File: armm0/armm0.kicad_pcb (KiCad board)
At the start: 2 copper layers, 25.4 x 52.1 mm, 20 parts, among them J1 Conn_02x10_Odd_Even, J4 Conn_02x08_Odd_Even, J5 Conn_02x08_Odd_Even, J6 Conn_01x05_Male, J7 Conn_01x05_Male, J8 Conn_01x03_Male, U1 STM32F070F6Px, U2 LD1117S33TR_SOT223

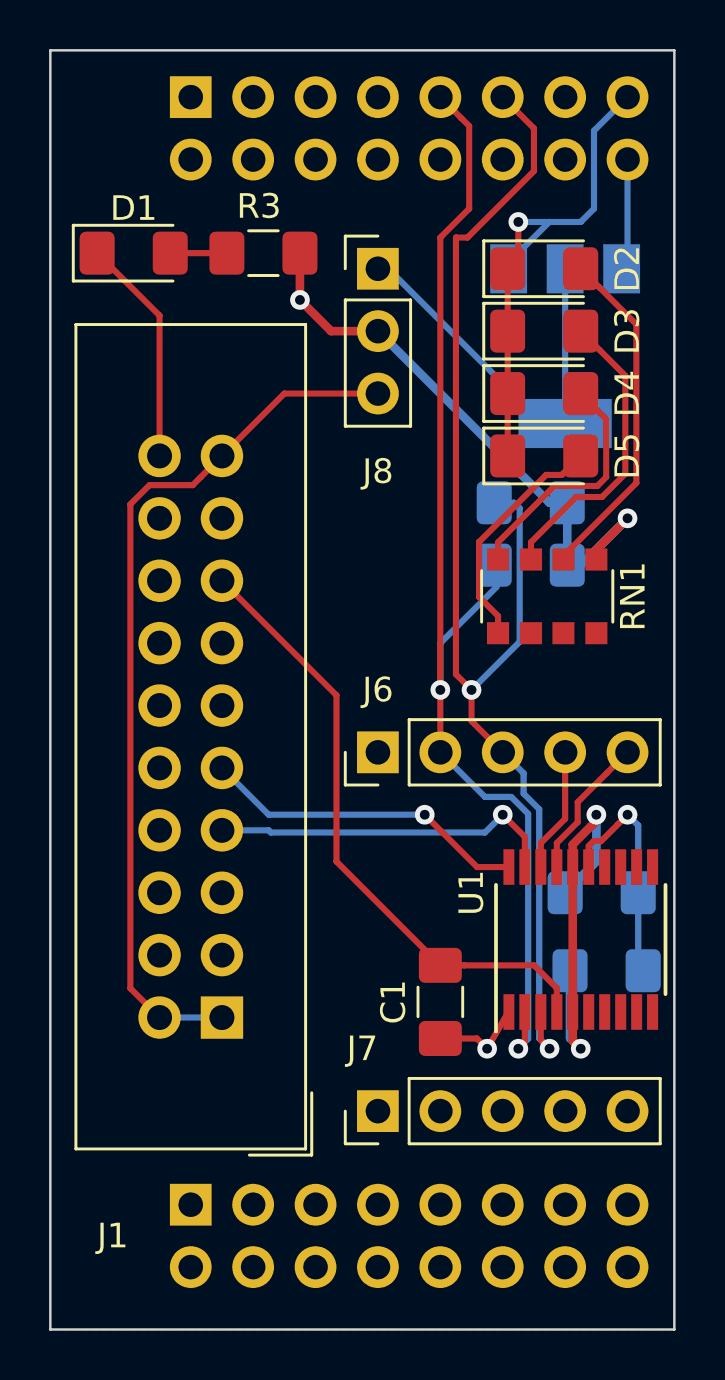
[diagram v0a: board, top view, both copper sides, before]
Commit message: pcb: Fixed header distance
Signed-off-by: Ben Lancaster <bdl@live.co.uk>
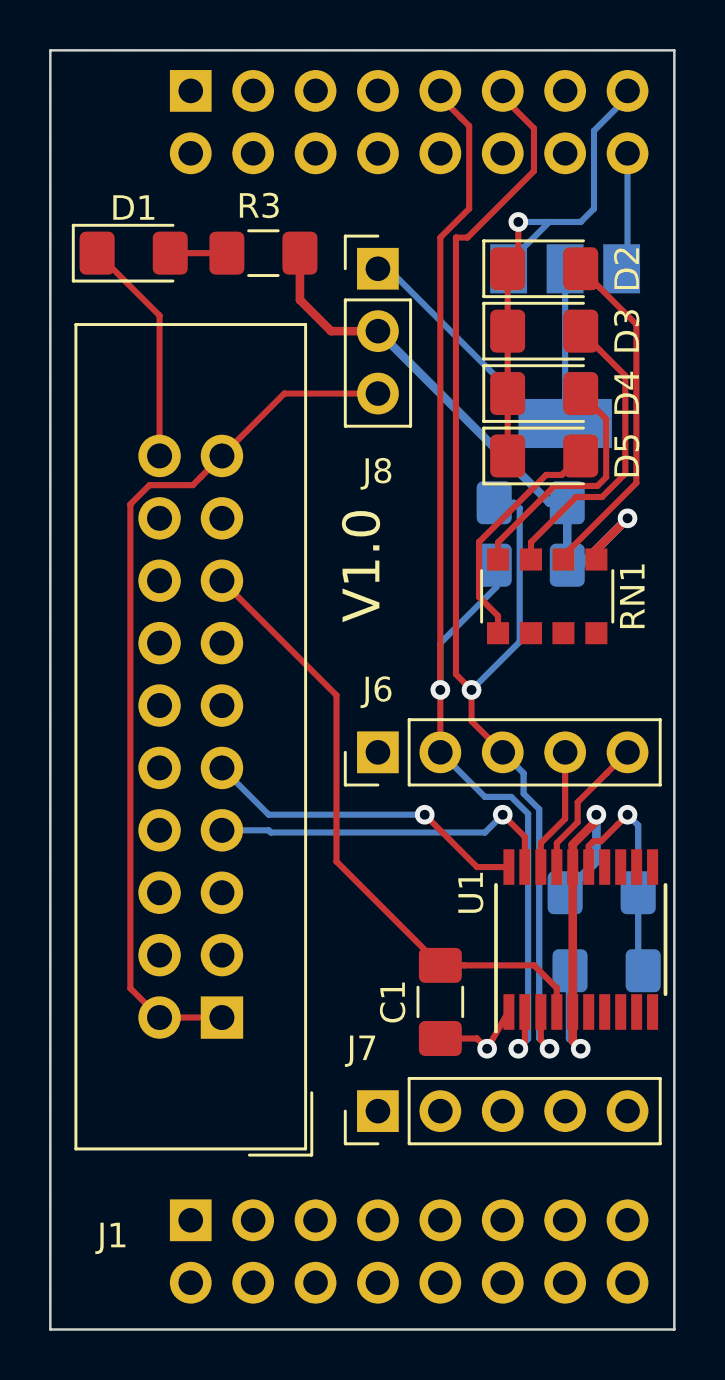
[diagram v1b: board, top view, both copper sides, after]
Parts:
- moved J4 0.63 mm to (80.6, 78.7)
- moved J5 0.25 mm to (80.6, 32.8)
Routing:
- net +3V3: vias 4 -> 3
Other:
- board text added: "BDL"
- board text added: "V1.0"
- board text removed: "+3v3"
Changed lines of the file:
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@@
   (general
     (thickness 1.6)
-    (drawings 12)
-    (tracks 170)
+    (drawings 14)
+    (tracks 169)
     (zones 0)
     (modules 20)
@@
     (34 B.Paste user)
     (35 F.Paste user)
-    (36 B.SilkS user hide)
+    (36 B.SilkS user)
     (37 F.SilkS user)
     (38 B.Mask user)
     (39 F.Mask user)
-    (40 Dwgs.User user)
+    (40 Dwgs.User user hide)
     (41 Cmts.User user)
     (42 Eco1.User user)
@@
   )
   (module Connector_PinHeader_2.54mm:PinHeader_2x08_P2.54mm_Vertical (layer B.Cu)
-    (at 80.645 33.02 270)
+    (at 80.645 32.766 270)
     (descr "Through hole straight pin header, 2x08, 2.54mm pitch, double rows")
     (tags "Through hole pin header THT 2x08 2.54mm double row")
@@
   )
   (module Connector_PinHeader_2.54mm:PinHeader_2x08_P2.54mm_Vertical (layer B.Cu)
-    (at 80.645 78.105 270)
+    (at 80.645 78.74 270)
     (descr "Through hole straight pin header, 2x08, 2.54mm pitch, double rows")
     (tags "Through hole pin header THT 2x08 2.54mm double row")
@@
     )
   )
+  (gr_text BDL (at 87.63 52.07 90) (layer B.SilkS)
+    (effects (font (size 1.5 1.5) (thickness 0.3)) (justify mirror))
+  )
+  (gr_text V1.0 (at 87.63 52.07 90) (layer F.SilkS)
+    (effects (font (size 1.5 1.5) (thickness 0.3)))
+  )
+  (dimension 48.514 (width 0.3) (layer Dwgs.User)
+    (gr_text "48.514 mm" (at 101.414 57.023 90) (layer Dwgs.User)
+      (effects (font (size 1.5 1.5) (thickness 0.3)))
+    )
+    (feature1 (pts (xy 98.552 32.766) (xy 99.900421 32.766)))
+    (feature2 (pts (xy 98.552 81.28) (xy 99.900421 81.28)))
+    (crossbar (pts (xy 99.314 81.28) (xy 99.314 32.766)))
+    (arrow1a (pts (xy 99.314 32.766) (xy 99.900421 33.892504)))
+    (arrow1b (pts (xy 99.314 32.766) (xy 98.727579 33.892504)))
+    (arrow2a (pts (xy 99.314 81.28) (xy 99.900421 80.153496)))
+    (arrow2b (pts (xy 99.314 81.28) (xy 98.727579 80.153496)))
+  )
   (gr_line (start 74.93 83.185) (end 100.33 83.185) (layer Edge.Cuts) (width 0.1))
   (gr_line (start 74.93 31.115) (end 74.93 83.185) (layer Edge.Cuts) (width 0.1))
@@
     (arrow2a (pts (xy 103.397986 31.115) (xy 102.811565 32.241504)))
     (arrow2b (pts (xy 103.397986 31.115) (xy 103.984407 32.241504)))
-  )
-  (gr_text +3v3 (at 74.295 49.53) (layer B.SilkS)
-    (effects (font (size 1.5 1.5) (thickness 0.3)) (justify mirror))
   )
   (gr_line (start 100.33 83.185) (end 24.13 83.185) (layer Eco1.User) (width 0.1))
@@
   (via (at 97.155 62.23) (size 0.8) (drill 0.4) (layers F.Cu B.Cu) (net 3))
   (segment (start 97.155 51.84) (end 97.155 51.435) (width 0.35) (layer F.Cu) (net 3))
-  (via (at 85.09 41.275) (size 0.8) (drill 0.4) (layers F.Cu B.Cu) (net 3))
   (segment (start 96.195 64.36) (end 96.195 70.26) (width 0.35) (layer F.Cu) (net 3))
   (segment (start 95.25 49.53) (end 95.9725 49.53) (width 0.35) (layer B.Cu) (net 3))
@@
   (segment (start 94.985 46.305) (end 88.685 40.005) (width 0.25) (layer B.Cu) (net 48))
   (segment (start 95.885 46.305) (end 94.985 46.305) (width 0.25) (layer B.Cu) (net 48))
-  (segment (start 79.375 70.485) (end 81.915 70.485) (width 0.25) (layer B.Cu) (net 54))
   (segment (start 84.455 45.085) (end 88.265 45.085) (width 0.25) (layer F.Cu) (net 54))
   (segment (start 81.915 47.625) (end 84.455 45.085) (width 0.25) (layer F.Cu) (net 54))
@@
   (segment (start 78.186399 69.296399) (end 78.186399 49.594471) (width 0.25) (layer F.Cu) (net 54))
   (segment (start 79.375 70.485) (end 78.186399 69.296399) (width 0.25) (layer F.Cu) (net 54))
+  (segment (start 79.375 70.485) (end 81.915 70.485) (width 0.25) (layer F.Cu) (net 54))
   (via (at 90.805 57.15) (size 0.8) (drill 0.4) (layers F.Cu B.Cu) (net 59))
   (segment (start 90.805 57.15) (end 90.805 59.69) (width 0.25) (layer F.Cu) (net 59))

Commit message: pcb: Removed name
Signed-off-by: Ben Lancaster <bdl@live.co.uk>
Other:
- board text removed: "BDL"
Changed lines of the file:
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@@
   (general
     (thickness 1.6)
-    (drawings 14)
+    (drawings 13)
     (tracks 169)
     (zones 0)
@@
     )
   )
-  (gr_text BDL (at 87.63 52.07 90) (layer B.SilkS)
-    (effects (font (size 1.5 1.5) (thickness 0.3)) (justify mirror))
-  )
   (gr_text V1.0 (at 87.63 52.07 90) (layer F.SilkS)

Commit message: sch: LED_DBUGn
Signed-off-by: Ben Lancaster <bdl@live.co.uk>
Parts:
- removed J7: Conn_01x05_Male, Connector_PinHeader_2.54mm:PinHeader_1x05_P2.54mm_Vertical
- removed RN1: R_Network04, Resistor_SMD:R_Array_Convex_4x1206
- added R4: 50, Resistor_SMD:R_0603_1608Metric_Pad1.05x0.95mm_HandSolder, F.Cu at (99.1, 51.0)
- added R5: 50, Resistor_SMD:R_0603_1608Metric_Pad1.05x0.95mm_HandSolder, F.Cu at (97.2, 51.0)
- added R6: 50, Resistor_SMD:R_0603_1608Metric_Pad1.05x0.95mm_HandSolder, F.Cu at (95.2, 51.0)
- added R7: 50, Resistor_SMD:R_0603_1608Metric_Pad1.05x0.95mm_HandSolder, F.Cu at (93.3, 51.0)
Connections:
- U1 pad 10: Net-(U1-Pad10) -> LED_DBUG1
- U1 pad 7: ADC_IN1 -> LED_DBUG4
- U1 pad 8: Net-(U1-Pad8) -> LED_DBUG3
- U1 pad 9: Net-(U1-Pad9) -> LED_DBUG2
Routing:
- net I2C1_SDA: track 50.2 -> 40.6 mm
- net Net-(D5-Pad2): track 9.62 -> 4.23 mm
- net Net-(D3-Pad2): track 12.3 -> 8.59 mm
- net LED_DBUG4: track 0.00 -> 3.48 mm, vias 0 -> 1
- net LED_DBUG3: track 0.00 -> 3.22 mm, vias 0 -> 1
- net Net-(D4-Pad2): track 10.0 -> 6.84 mm
- net LED_DBUG2: track 0.00 -> 2.96 mm, vias 0 -> 1
- net Net-(D2-Pad2): track 14.0 -> 11.2 mm
- net LED_DBUG1: track 0.00 -> 2.70 mm, vias 0 -> 1
- net +3V3: track 41.3 -> 39.1 mm, vias 3 -> 2

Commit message: pcb: Connected LEDs and I2Cs
Signed-off-by: Ben Lancaster <bdl@live.co.uk>
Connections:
- R4 pad 1: LED_DBUG1 -> LED_DBUG4
- R5 pad 1: LED_DBUG2 -> LED_DBUG3
- R6 pad 1: LED_DBUG3 -> LED_DBUG2
- R7 pad 1: LED_DBUG4 -> LED_DBUG1
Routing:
- net LED_DBUG1: track 2.70 -> 48.8 mm, vias 1 -> 2
- net LED_DBUG2: track 2.96 -> 46.9 mm, vias 1 -> 2
- net LED_DBUG3: track 3.22 -> 44.9 mm, vias 1 -> 2
- net LED_DBUG4: track 3.48 -> 43.0 mm, vias 1 -> 2
- net +3V3: track 39.1 -> 52.2 mm, vias 2 -> 3
- net I2C1_SDA: track 40.6 -> 48.4 mm
- net I2C1_SCL: track 53.4 -> 47.9 mm
- net GND: track 44.1 -> 46.3 mm, vias 3 -> 4

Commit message: pcb: Flip stlink connector to prevent clash with 5 pin header
Signed-off-by: Ben <bdl@live.co.uk>
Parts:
- moved J1 24.3 mm to (78.7, 46.4), turned to 0 degrees
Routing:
- net SWDIO: track 14.3 -> 21.4 mm
- net SWCLK: track 13.9 -> 19.7 mm
- net GND: track 46.3 -> 42.1 mm, vias 4 -> 5
- net NRST: track 25.4 -> 21.3 mm, vias 0 -> 1
- net STLINK_3V3: track 35.9 -> 34.5 mm
- net I2C1_SCL: track 47.9 -> 46.7 mm

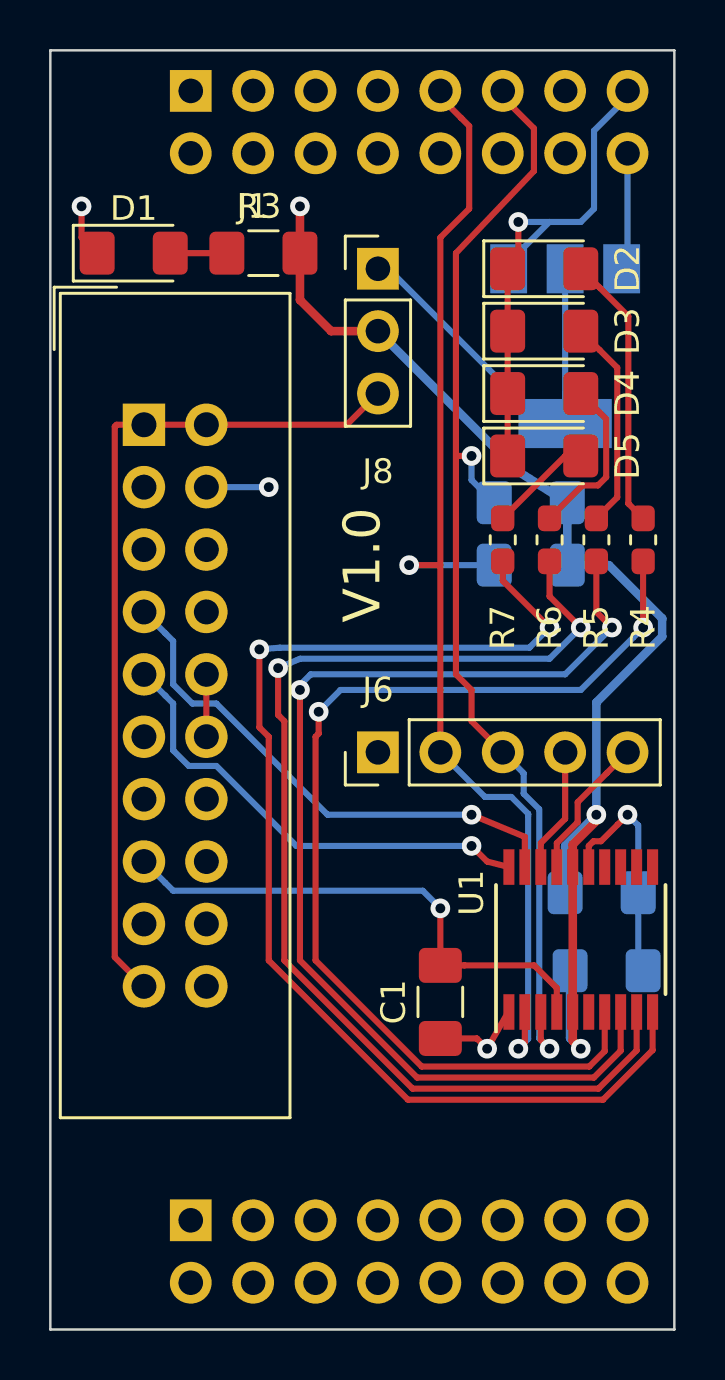
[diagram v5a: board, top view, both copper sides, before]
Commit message: pcb: Resize to exactly 1x2 inches to save on costs
Signed-off-by: Ben Lancaster <bdl@live.co.uk>
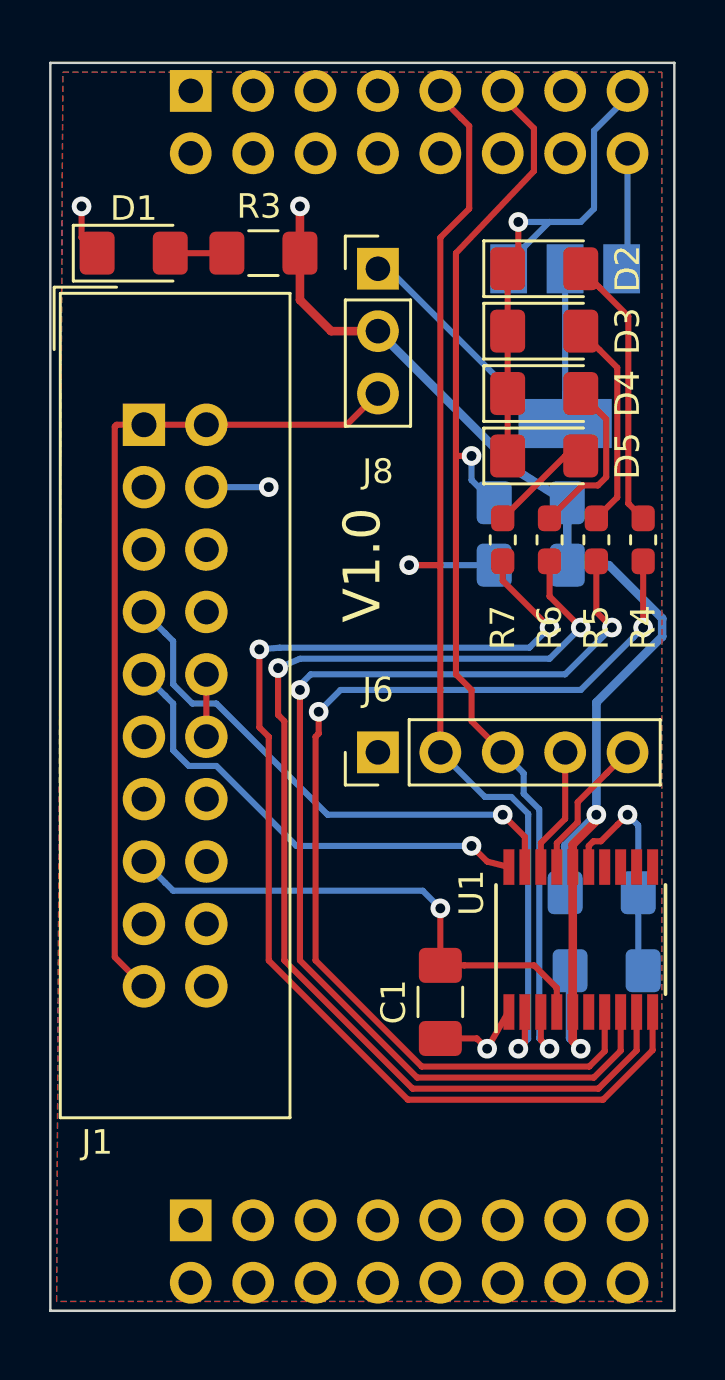
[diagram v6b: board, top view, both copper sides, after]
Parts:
- R3: value R -> 100
- R4, R5, R6, R7: value 50 -> 100
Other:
- board size 25.4 x 52.1 mm -> 25.4 x 50.8 mm
